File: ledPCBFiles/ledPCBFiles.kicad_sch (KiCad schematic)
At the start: 12 parts, among them U1 LM555xN, U2 74LS161

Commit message: Finished connecting 555 timer to 74LS161
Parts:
- added C2: C_Small, symbol Device:C_Small
- added R6: 1000, symbol Device:R_US
- R1: value 10k -> 100k
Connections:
- net +6V: now also R1.1, U2.1 (~{MR})
- net GND: now also C2.2
- net at R1.2: now also U1.7 (DISCH), R6.2
- net at U1.2 (TRIG): now also C2.1, R6.1
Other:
- moved on the sheet: C1, R1

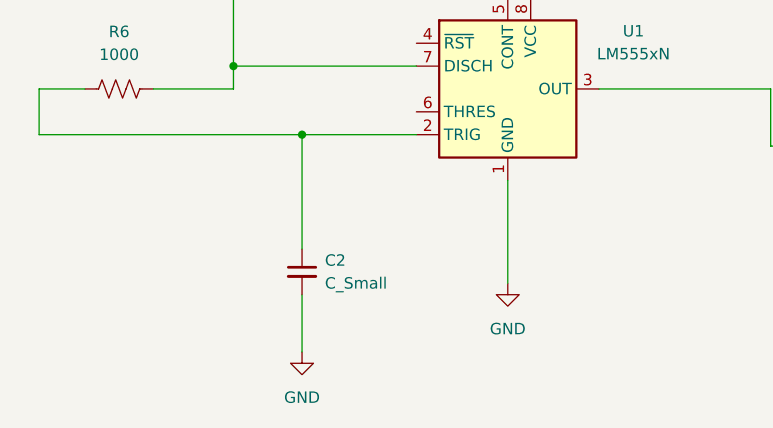
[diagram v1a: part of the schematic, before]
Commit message: Changed value of trigger capacitor
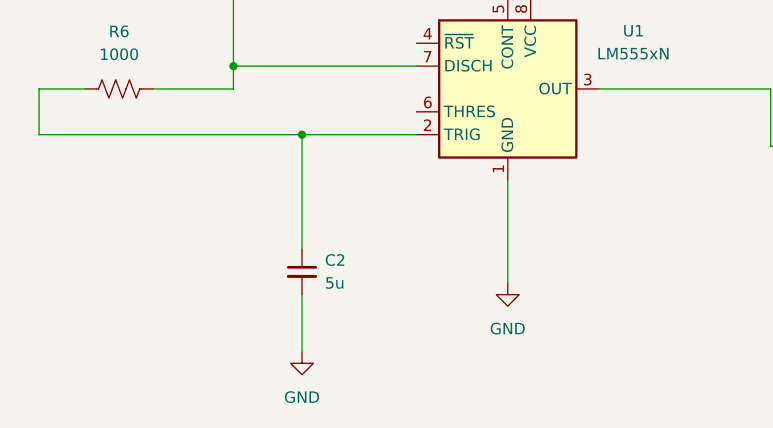
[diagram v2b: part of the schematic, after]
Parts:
- C2: value C_Small -> 5u
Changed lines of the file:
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@@
 			)
 		)
-		(property "Value" "C_Small"
+		(property "Value" "5u"
 			(at 99.06 105.4162 0)
 			(show_name no)
